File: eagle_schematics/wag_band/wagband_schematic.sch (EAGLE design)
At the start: 13 parts, among them U2 TLV1117-33CDCY

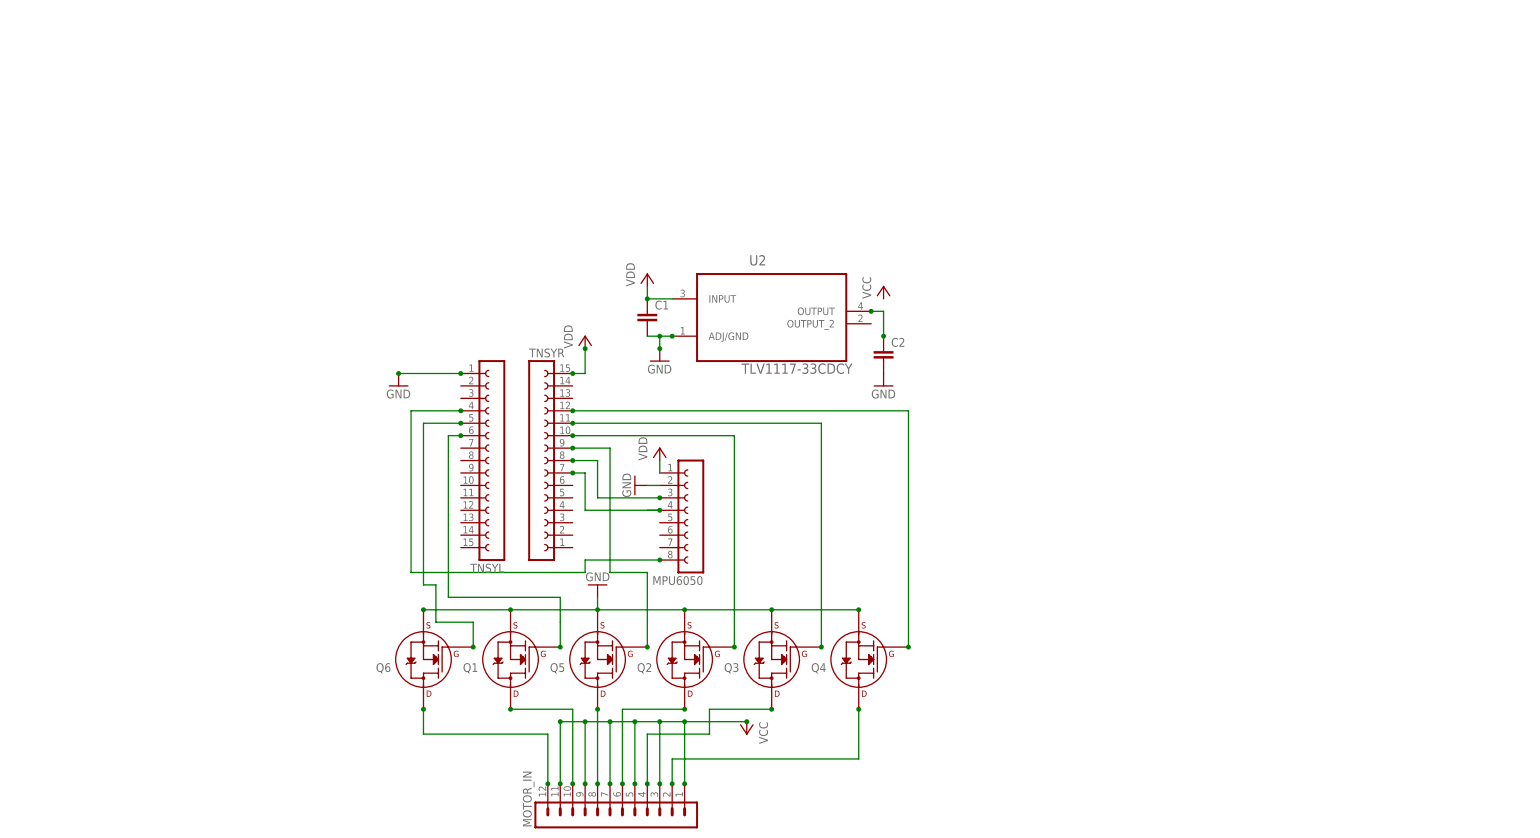
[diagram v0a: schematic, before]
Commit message: Added schematics and PCB layout to the repo
This commit includes the major schematic and board for the PCB for a
single WAG band (Not the center band or the one with all the flex
sensors). The schematic is pretty much done although the board needs to
be flipped around as it is upside for PCB printing.
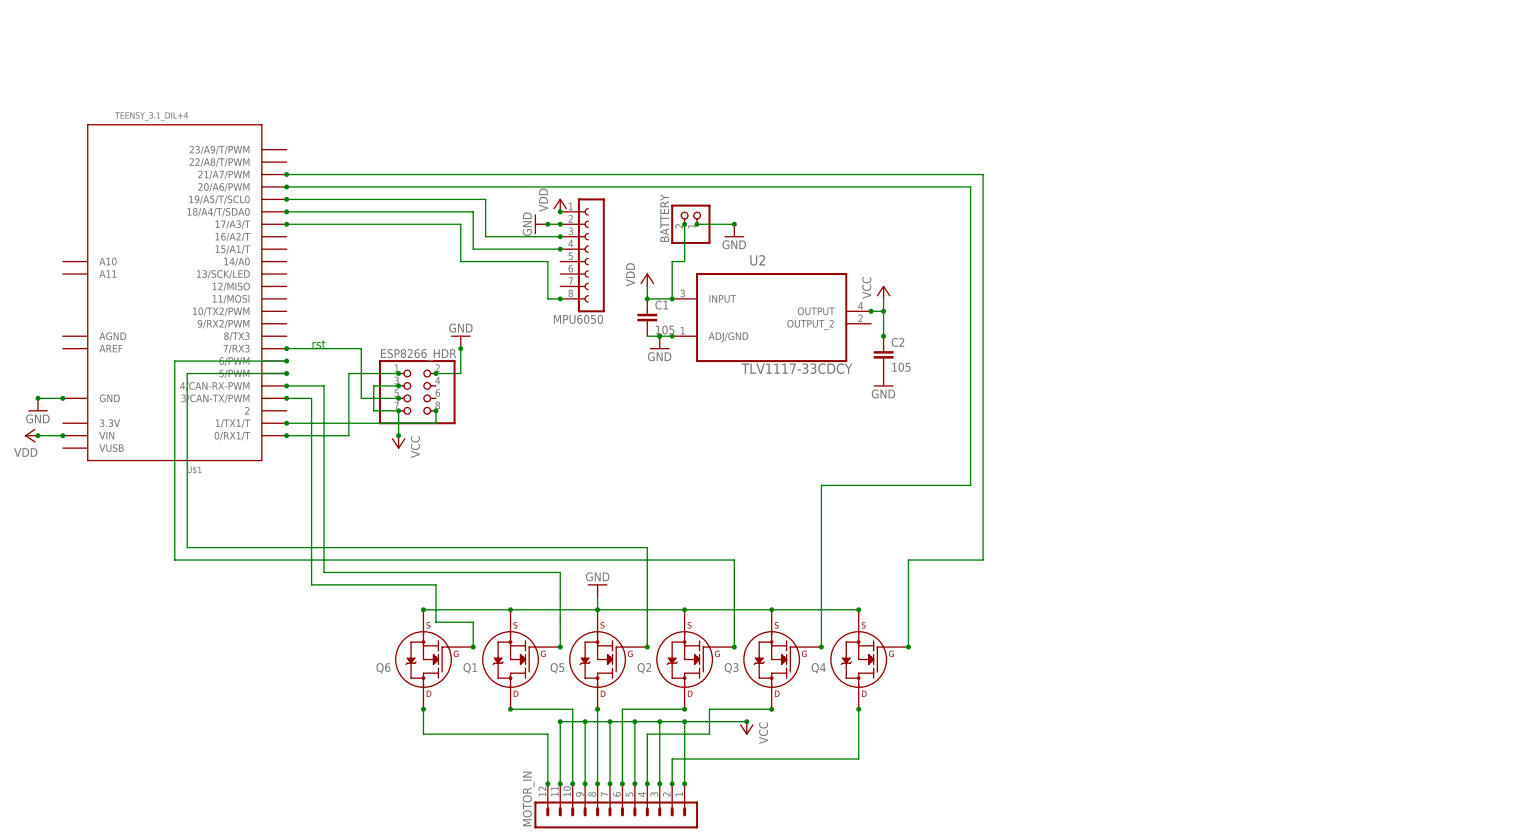
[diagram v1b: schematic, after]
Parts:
- removed TNSYL, TNSYR: (no value), con-lsta:FE15-1
- added BATTERY: (no value), adafruit:JST_2PIN-THM-RA
- added ESP8266_HDR: (no value), pinhead:PINHD-2X4
- added U$1: TEENSY_3.1_DIL+4, Teensy_3_and_LC_Series_Boards_v1.1:TEENSY_3.1_DIL+4
- C1, C2: value (none) -> 105
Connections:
- removed net N$12: Q1.G
- removed net N$18: MPU6050.4, TNSYR.7
- new net N$19: ESP8266_HDR.8, U$1.1/TX1/T
- new net N$21: ESP8266_HDR.5, U$1.7/RX3
- new net N$4: MPU6050.4, U$1.18/A4/T/SDA0
- net GND: now also BATTERY.2, ESP8266_HDR.2, U$1.GND; no longer TNSYL.1
- net N$1: now also U$1.21/A7/PWM; no longer TNSYR.12
- net N$16: now also U$1.5/PWM; no longer TNSYR.9
- net N$17: now also U$1.19/A5/T/SCL0; no longer TNSYR.8
- net N$2: now also U$1.6/PWM; no longer TNSYR.10
- net N$3: now also U$1.20/A6/PWM; no longer TNSYR.11
- net N$5: now also U$1.3/CAN-TX/PWM; no longer TNSYL.5
- net N$6: now also Q1.G, U$1.4/CAN-RX-PWM; no longer TNSYL.6
- net N$7: now also ESP8266_HDR.1, U$1.0/RX1/T; no longer MPU6050.8, TNSYL.4
- net N$8: now also MPU6050.8, U$1.17/A3/T; no longer C2.1, U2.OUTPUT
- net VCC: now also BATTERY.1, C2.1, ESP8266_HDR.3, ESP8266_HDR.7, U$1.VIN, U2.OUTPUT; no longer TNSYR.15
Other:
- note added: "rst"
- moved on the sheet: MPU6050

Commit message: Added more parts for eagle
Finished PCBs
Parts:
- removed BATTERY: (no value), adafruit:JST_2PIN-THM-RA
- removed ESP8266_HDR: (no value), pinhead:PINHD-2X4
- removed MPU6050: (no value), con-lsta:FE08-1
- added BAT, CHGR: (no value), adafruit:JST_2PIN-THM-RA
- added JP1: (no value), mqp_custom_parts:MPU6050_BREAKOUT
- added LED1, PWR: (no value), led:LED5MM
- added Q7, Q8: (no value), mqp_custom_parts:TRANSISTOR_NPNMMBT3904
- added R1, R5: 1k, resistor:R-US_R1206
- added R2, R3: 30k, resistor:R-US_R1206
- added R4: 10k, resistor:R-US_R1206
- added U$2: ESP01, esp8266modules:ESP01
- added U$3: CB10LV103M, mqp_custom_parts:CB10LV103M
- added U$4: MS12ASW13, mqp_custom_parts:MS12ASW13
- added U1: LM358DR, Texas Instruments_By_element14_Batch_1:LM358DR
- C1, C2: device rcl:C-EU025-024X044 -> resistor:C-USC0805K
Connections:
- new net N$12: U$1.8/TX3, U$2.RXD
- new net N$18: U$1.11/MOSI, U$2.GPIO2
- new net N$20: Q7.C, R1.1, U1.1IN+
- new net N$22: LED1.C, R1.2
- new net N$23: Q7.B, Q8.C, R2.1
- new net N$24: R4.2, U$1.9/RX2/PWM, U$2.CH_PD
- new net N$25: Q8.B, U$3.C, U1.1IN-
- new net N$26: U$1.12/MISO, U1.1OUT
- new net N$27: R3.1, U$3.B
- new net N$28: BAT.2, U$4.P$2
- new net N$29: CHGR.2, U$4.P$1
- net GND: now also BAT.1, CHGR.1, JP1.GND, Q7.E, Q8.E, R5.1, U$1.AGND, U$2.GND, U$3.A, U1.GND; no longer BATTERY.2, ESP8266_HDR.2, MPU6050.2
- net N$1: now also U$1.23/A9/T/PWM; no longer U$1.21/A7/PWM
- net N$17: now also JP1.SCL; no longer MPU6050.3
- net N$19: now also U$1.10/TX2/PWM, U$2.GPIO0; no longer ESP8266_HDR.8, U$1.1/TX1/T
- net N$21: now also PWR.C, R5.2; no longer ESP8266_HDR.5, U$1.7/RX3
- net N$3: now also U$1.22/A8/T/PWM; no longer U$1.20/A6/PWM
- net N$4: now also JP1.SDA; no longer MPU6050.4
- net N$7: now also U$1.7/RX3, U$2.TXD; no longer ESP8266_HDR.1, U$1.0/RX1/T
- net N$8: now also JP1.INT; no longer MPU6050.8
- net VCC: now also JP1.VCC, LED1.A, PWR.A, R2.2, R3.2, R4.1, U$2.RST, U$2.VCC, U$4.P$3, U1.VCC; no longer BATTERY.1, ESP8266_HDR.3, ESP8266_HDR.7, MPU6050.1
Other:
- note added: "WAG Band Design Chas Frick Wearable Haptic MQP 2015-2016"
- note removed: "rst"
- moved on the sheet: C1, C2, MOTOR_IN, Q1, Q2, Q3, Q4, Q5, Q6, U$1, U2
